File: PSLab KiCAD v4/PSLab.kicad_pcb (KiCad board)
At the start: 4 copper layers, 101.6 x 53.3 mm, 140 parts, among them CON1 USB-MICRO-B, J1 Programmer, J12 Sensors, J2 SQRs, J3 LA, J4 OSC_Pins, J5 Sin, J6 I2C, J7 IDs, J8 TX_RX_ES, J9 Test_Vs, P1 Power_Sources, P7 NRF, Q1 MMBT3906, Q2 MMBT3904, Q3 MMBT3906, U1 MCP2200, U10 TL082, U11 6S21, U12 6S21, U13 TL082, U15 ESP8266, U16 TL082, U2 74HC126, U3 PIC24EP256GP204, U4 TC1240A, U5 7660, U6 LM1117-3.3, U7 LM324, U8 TL082, U9 MCP4728, X1 12MHz

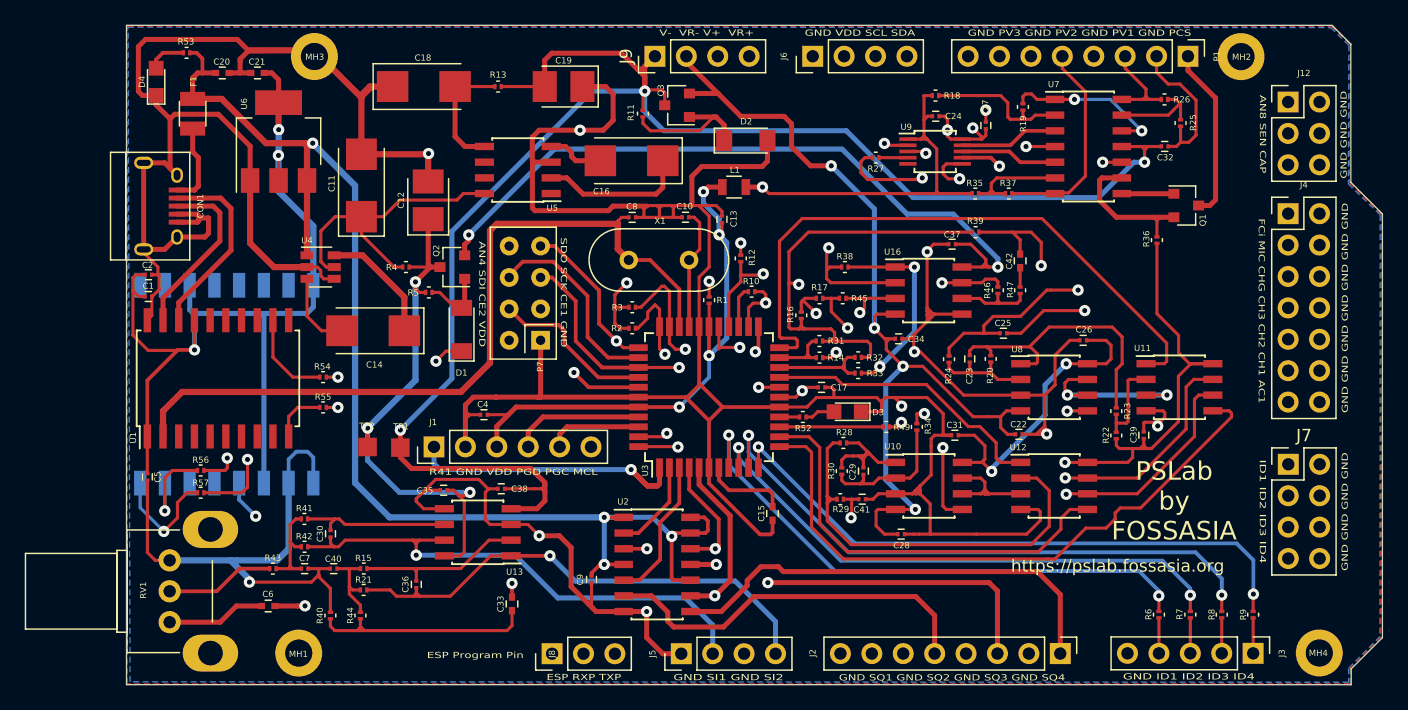
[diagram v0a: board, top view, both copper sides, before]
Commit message: Optimizing layout
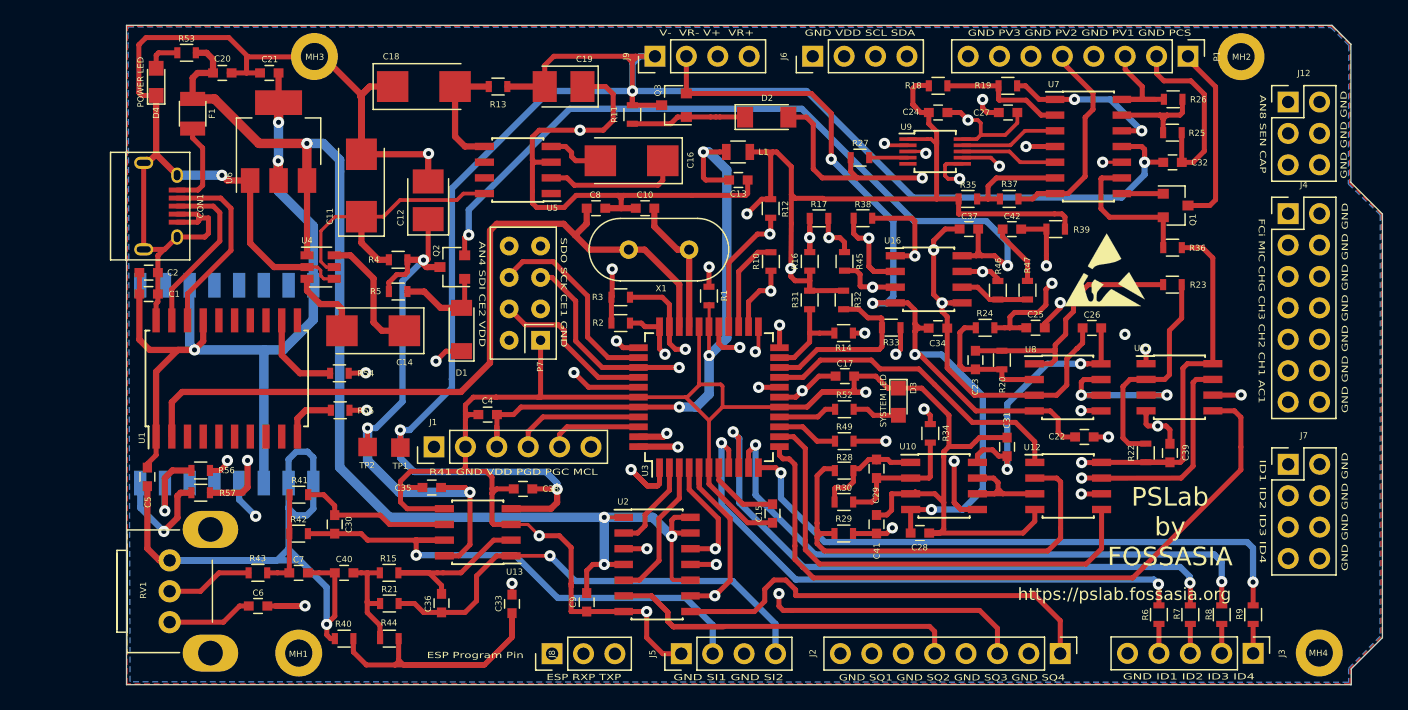
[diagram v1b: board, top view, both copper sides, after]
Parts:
- added REF***: ESD-Logo_6.6x6mm_SilkScreen, Symbols:ESD-Logo_6.6x6mm_SilkScreen, F.Cu at (170.1, 80.0)
- C1, C10, C13, C17, C2, C22, C23, C24, C25, C26, C27, C28, C29, C30, C31, C32, C34, C35, C36, C37, C38, C39, C4, C40, C41, C5, C7, C8, C9: footprint Capacitors_SMD:C_0201 -> Capacitors_SMD:C_0603
- C15, C20, C21, C33, C42, C6: footprint Capacitors_SMD:C_0402 -> Capacitors_SMD:C_0603
- R1, R10, R11, R12, R13, R14, R15, R16, R17, R18, R19, R2, R20, R21, R22, R23, R24, R25, R26, R27, R28, R29, R3, R30, R31, R32, R33, R34, R35, R36, R37, R38, R39, R4, R40, R41, R42, R43, R44, R45, R46, R47, R49, R5, R52, R53, R54, R55, R56, R57, R6, R7, R8, R9: footprint Resistors_SMD:R_0201 -> Resistors_SMD:R_0603
- moved R23 11.2 mm to (175.5, 81.2), turned to 180 degrees
- moved R39 6.48 mm to (166.1, 76.7), turned to 0 degrees
- moved R17 6.47 mm to (147.0, 75.9)
- moved C22 5.30 mm to (168.4, 93.5)
- moved R32 4.79 mm to (148.9, 82.5), turned to 90 degrees
- moved R12 4.71 mm to (143.1, 75.1)
- moved R33 4.55 mm to (152.8, 84.7)
- moved R16 4.41 mm to (146.2, 79.3)
- moved C31 4.32 mm to (162.2, 94.3), turned to 270 degrees
- moved R38 4.21 mm to (150.5, 75.8)
- moved D3 4.18 mm to (153.4, 90.7), turned to 270 degrees
- moved R24 3.87 mm to (160.4, 84.7), turned to 180 degrees
- moved R49 3.59 mm to (149.0, 93.9)
- moved C13 3.45 mm to (140.4, 72.8), turned to 180 degrees
- moved R52 3.42 mm to (149.0, 91.3)
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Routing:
- net /RxD: track 95.0 -> 160.1 mm
- net V-: track 151.1 -> 193.8 mm, vias 3 -> 4
- net /ID4: track 93.5 -> 52.0 mm
- net /ID1: track 84.7 -> 47.0 mm
- net /ID2: track 86.7 -> 50.3 mm
- net /TxD: track 87.4 -> 122.4 mm
- net /ESPROG: track 33.6 -> 64.6 mm
- net SDA: track 79.2 -> 52.1 mm
- net SINE1: track 42.6 -> 68.5 mm
- net Vdd: track 232.7 -> 258.5 mm, vias 8 -> 7
- net VR-: track 86.0 -> 103.4 mm
- net GND: track 804.2 -> 820.8 mm
- net V+: track 117.2 -> 133.5 mm
- net SCL: track 65.4 -> 49.7 mm
- net /SQR2: track 59.6 -> 45.4 mm
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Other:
- board text added: "ESP8266"
- board text added: "POWER LED"
- board text added: "SYSTEM LED"

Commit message: Programmer pin header adjustments
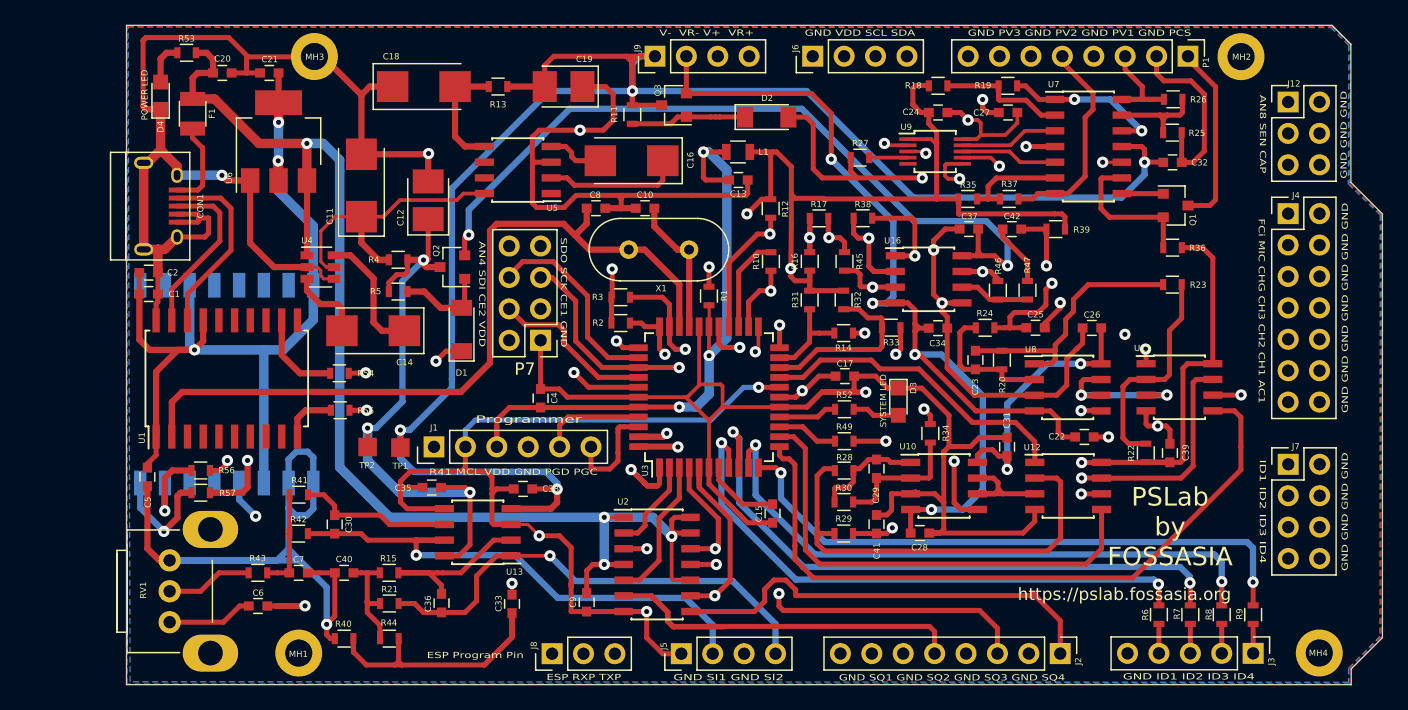
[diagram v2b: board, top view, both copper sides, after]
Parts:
- removed REF***: ESD-Logo_6.6x6mm_SilkScreen, Symbols:ESD-Logo_6.6x6mm_SilkScreen
- P7: footprint Custom_Components:nRF24L01_Breakout_2 -> Pin_Headers:Pin_Header_Straight_2x04_Pitch2.54mm
- moved C4 4.48 mm to (124.4, 90.4), turned to 90 degrees
- moved D4 1.18 mm to (93.7, 65.9)
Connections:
- J1 pad 2: GND -> MCLR
- J1 pad 4: PGD2 -> GND
- J1 pad 5: PGC2 -> PGD2
- J1 pad 6: MCLR -> PGC2
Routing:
- net MCLR: track 33.1 -> 45.6 mm
- net Net-(C33-Pad2): track 31.7 -> 25.0 mm
- net PGD2: track 10.6 -> 8.40 mm
- net PGC2: track 9.56 -> 8.61 mm
- net GND: track 820.8 -> 821.7 mm
- net Net-(D4-Pad2): track 2.84 -> 3.44 mm
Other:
- board text added: "Programmer"
- board text added: "R41 MCL VDD GND PGD PGC"
- board text removed: "R41 GND VDD PGD PGC MCL"

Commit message: Ran DRC Check on layout
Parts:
- moved C4 1.42 mm to (123.0, 90.3), turned to 0 degrees
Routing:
- net /ESPROG: track 64.6 -> 38.0 mm
- net Vdd: track 258.2 -> 239.2 mm
- net GND: track 821.7 -> 810.3 mm
- net /RxD: track 160.1 -> 153.9 mm
- net SDO: track 86.8 -> 83.7 mm
- net MCLR: track 45.6 -> 42.9 mm
- net SQ4: track 59.6 -> 57.2 mm
- net Net-(C33-Pad2): track 25.0 -> 23.0 mm
- net /TxD: track 122.4 -> 124.1 mm
- net Net-(R16-Pad1): track 57.4 -> 55.8 mm
- net PVS1: track 10.2 -> 9.12 mm
- net Net-(U11-Pad3): track 13.4 -> 13.9 mm
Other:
- rule trace_min: 0.254 -> 0.1524
- board text added: "ICSP Programmer"
- board text added: "NRF24"
- board text removed: "Programmer"

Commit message: Added Gerber files
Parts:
- removed TP1, TP2: TEST, Measurement_Points:Measurement_Point_Square-SMD-Pad_Small
- added t_0V: TEST, Measurement_Points:Measurement_Point_Round-SMD-Pad_Small, F.Cu at (107.9, 94.3)
- added t_5V: TEST, Measurement_Points:Measurement_Point_Round-SMD-Pad_Small, F.Cu at (127.6, 100.0)
- added t_V+: TEST, Measurement_Points:Measurement_Point_Round-SMD-Pad_Small, F.Cu at (110.4, 94.2)
- added t_V-: TEST, Measurement_Points:Measurement_Point_Round-SMD-Pad_Small, F.Cu at (113.1, 94.3)
- RV1: value 47K -> 100K
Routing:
- net GND: track 810.3 -> 818.2 mm
- net +5V: track 116.3 -> 123.3 mm
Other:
- rule trace_min: 0.1524 -> 0.15
- rule via_min_size: 0.3 -> 0.5
- board text added: "4th Rev @ 23 Jan 17"
- board text removed: "4th Rev @ 11 Jan 17"

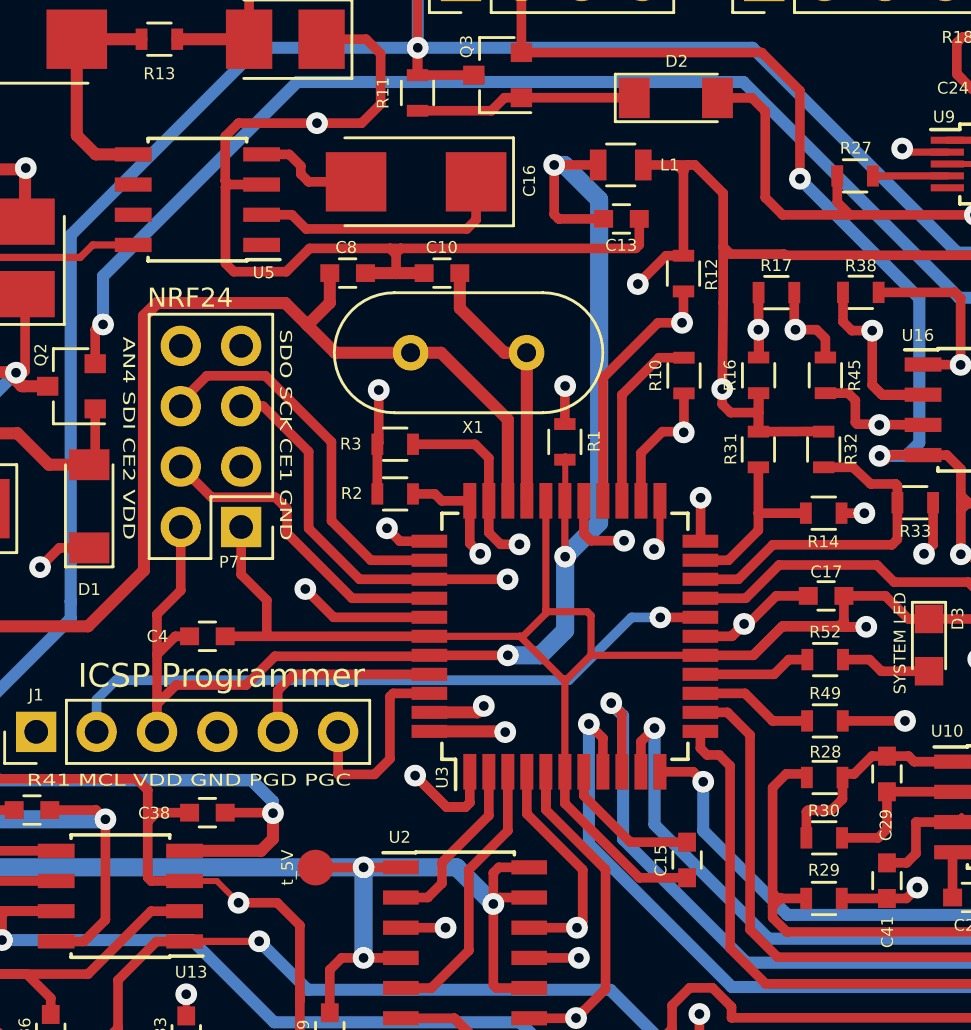
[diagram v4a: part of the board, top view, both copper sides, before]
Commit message: Added breakouts for MCP2200
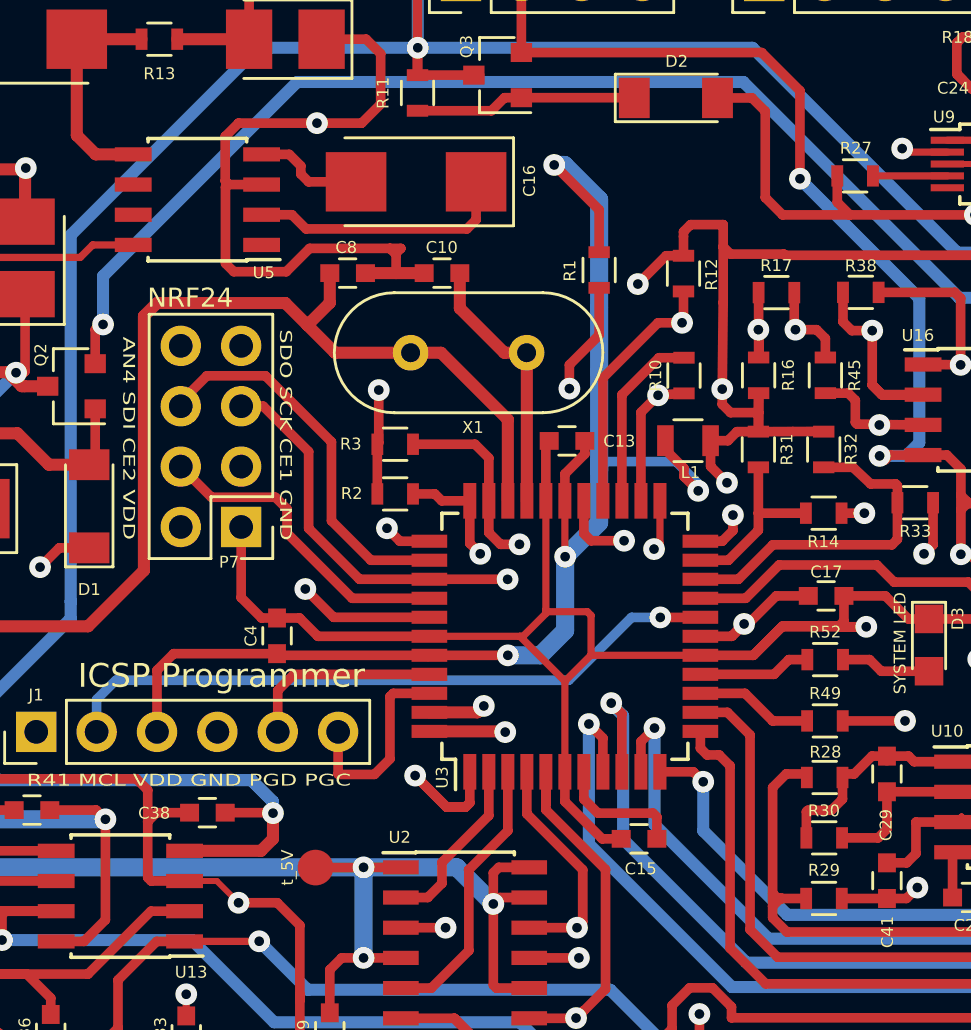
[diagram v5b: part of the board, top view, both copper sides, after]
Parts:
- moved L1 11.9 mm to (143.2, 82.1)
- moved C13 9.62 mm to (138.2, 82.1), turned to 0 degrees
- moved R1 7.37 mm to (139.5, 74.9), turned to 270 degrees
- moved C4 2.93 mm to (126.0, 90.3), turned to 90 degrees
- moved C15 2.21 mm to (141.2, 98.8), turned to 180 degrees
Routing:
- net GND: track 818.2 -> 804.0 mm
- net AVdd: track 170.3 -> 175.8 mm, vias 5 -> 6
- net MCLR: track 42.9 -> 45.8 mm
- net /CAP: track 54.2 -> 53.0 mm
- net Vdd: track 239.2 -> 238.4 mm, vias 7 -> 8
- net Net-(C15-Pad1): track 6.16 -> 5.45 mm
